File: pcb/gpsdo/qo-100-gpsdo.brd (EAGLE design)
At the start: 100 x 69.5 mm, 272 parts, among them CON1 3P-SH-SIDE, CON2 4P-SH-TOP, CON3 3P-SH-TOP, CON4 2EDG-2P-5MM, J1 DCJACK, U1 EFM32GG11B420F2048GL112, U10 AD9544, U11 74LVC1G17, U12 74LVC1G17, U13 74LVC1G17, U14 74LVC1G17, U15 74LVC1G17, U16 ADM7171ACPZ-1.8, U17 ADM7171ACPZ-5.0, U18 MIC23155, U19 LT8636, U2 74LVC1G17, U20 ADM7171ACPZ-3.3, U3 74LVC1G17, U4 MAX-M8Q, U5 MCP1501-40, U6 AD5541ACPZ, U7 MCP6V31, U8 OSC5A2B02, U9 DSB321SDA

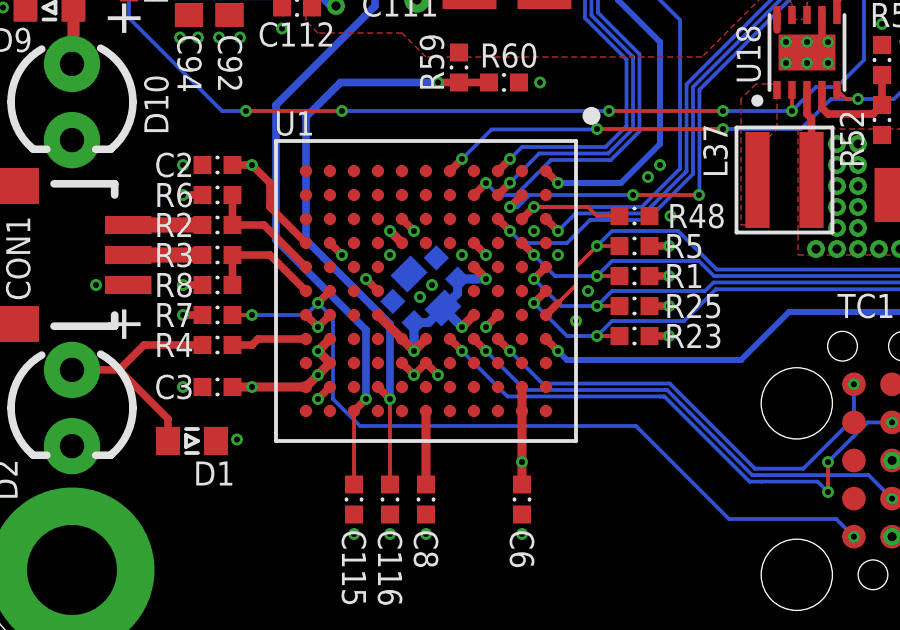
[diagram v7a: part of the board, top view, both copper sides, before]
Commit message: GPSDO production files
Signed-off-by: João Silva <jgc3silva@gmail.com>
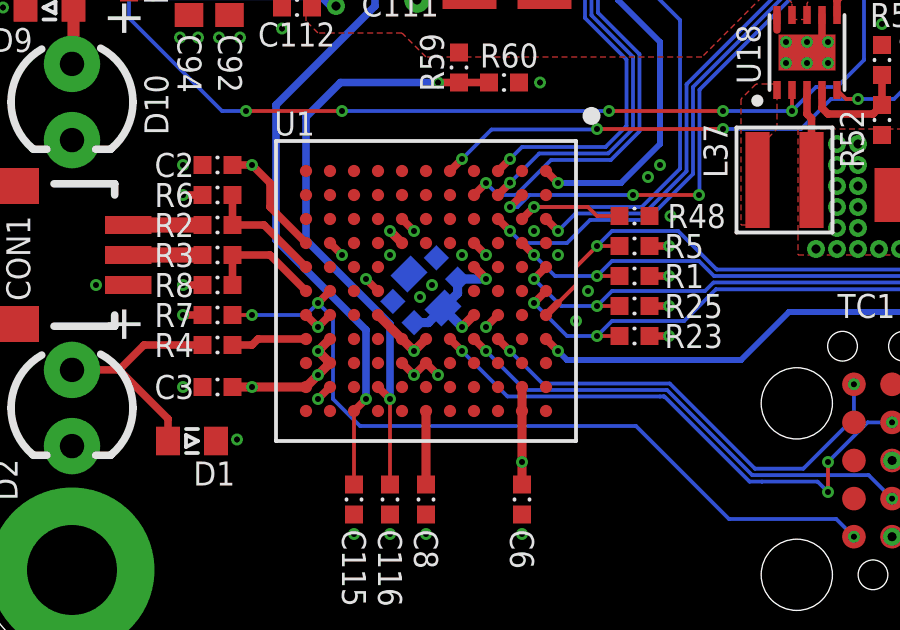
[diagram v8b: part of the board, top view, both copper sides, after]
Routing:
- net 3V3: track 140.3 -> 139.4 mm
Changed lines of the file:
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@@
 <drawing>
 <settings>
-<setting alwaysvectorfont="yes"/>
+<setting alwaysvectorfont="no"/>
 <setting verticaltext="up"/>
 </settings>
@@
 <via x="14.4" y="10.3" extent="1-16" drill="0.2"/>
 <wire x1="14.8" y1="10.7" x2="14.4" y2="10.3" width="0.3048" layer="1"/>
-<wire x1="14.4" y1="10.3" x2="14.4" y2="11.242890625" width="0.3048" layer="16"/>
-<wire x1="14.4" y1="11.242890625" x2="14.403553125" y2="11.24644375" width="0.3048" layer="16"/>
-<wire x1="14.403553125" y1="11.24644375" x2="14.87781875" y2="11.24644375" width="0.3048" layer="16"/>
 <wire x1="14.87781875" y1="11.24644375" x2="15.3656875" y2="11.7343125" width="0.3048" layer="16"/>
 <wire x1="15.853553125" y1="12.69644375" x2="15.853553125" y2="12.222178125" width="0.3048" layer="16"/>
@@
 <via x="16.8" y="12.7" extent="1-16" drill="0.2"/>
 <wire x1="15.853553125" y1="12.69644375" x2="15.857109375" y2="12.7" width="0.3048" layer="16"/>
-<wire x1="15.857109375" y1="12.7" x2="16.8" y2="12.7" width="0.3048" layer="16"/>
+<wire x1="15.85355625" y1="12.69644375" x2="15.8571125" y2="12.7" width="0.3048" layer="16"/>
+<wire x1="15.8571125" y1="12.7" x2="16.8" y2="12.7" width="0.3048" layer="16"/>
+<wire x1="14.40355625" y1="11.24644375" x2="14.87781875" y2="11.24644375" width="0.3048" layer="16"/>
 </signal>
 <signal name="GPS_BIAS_INT">
